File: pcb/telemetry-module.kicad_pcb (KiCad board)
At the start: 2 copper layers, 45.5 x 30 mm, 8 parts, among them J1 ODU Diagnostic Port, J3 5V-3.3V Level Shifter, J4 XIAO ESP32S3, J5 ODU 5V power jumper

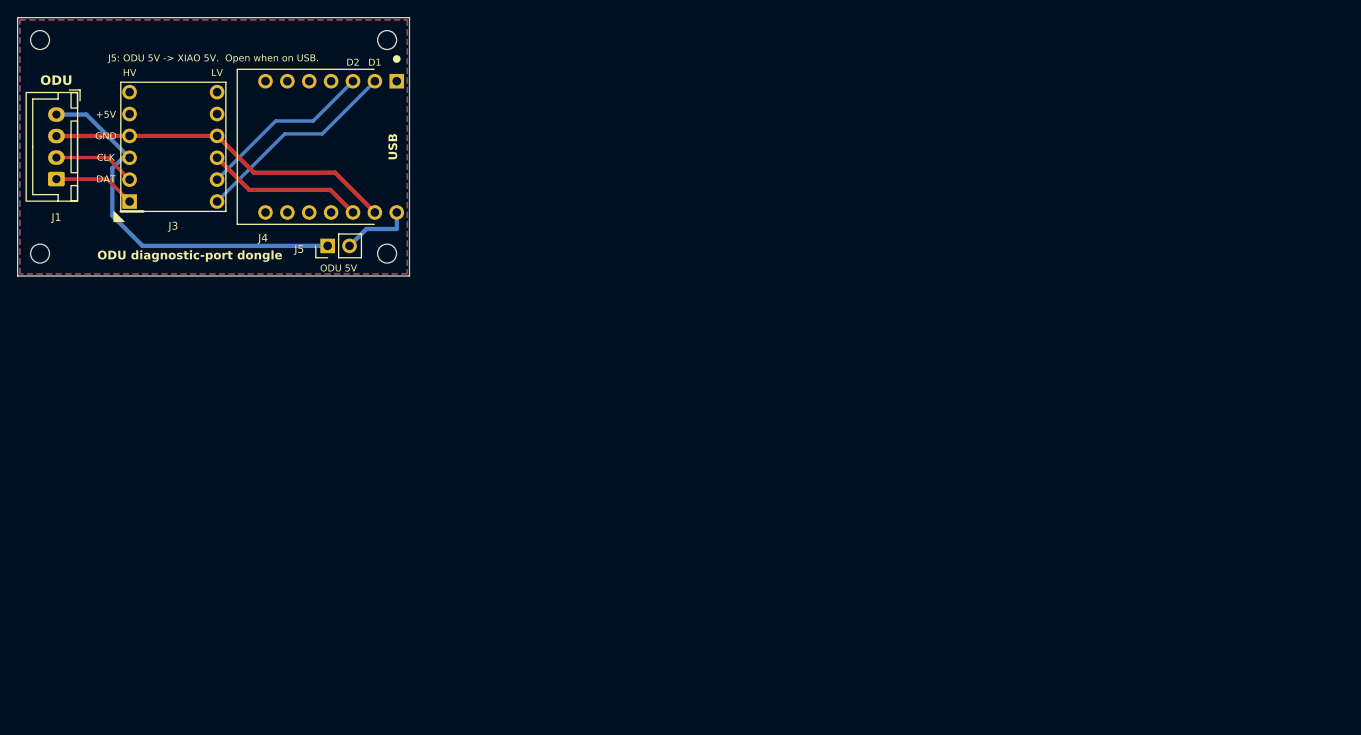
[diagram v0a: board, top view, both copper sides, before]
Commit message: GH-0014: reduce size of PCB
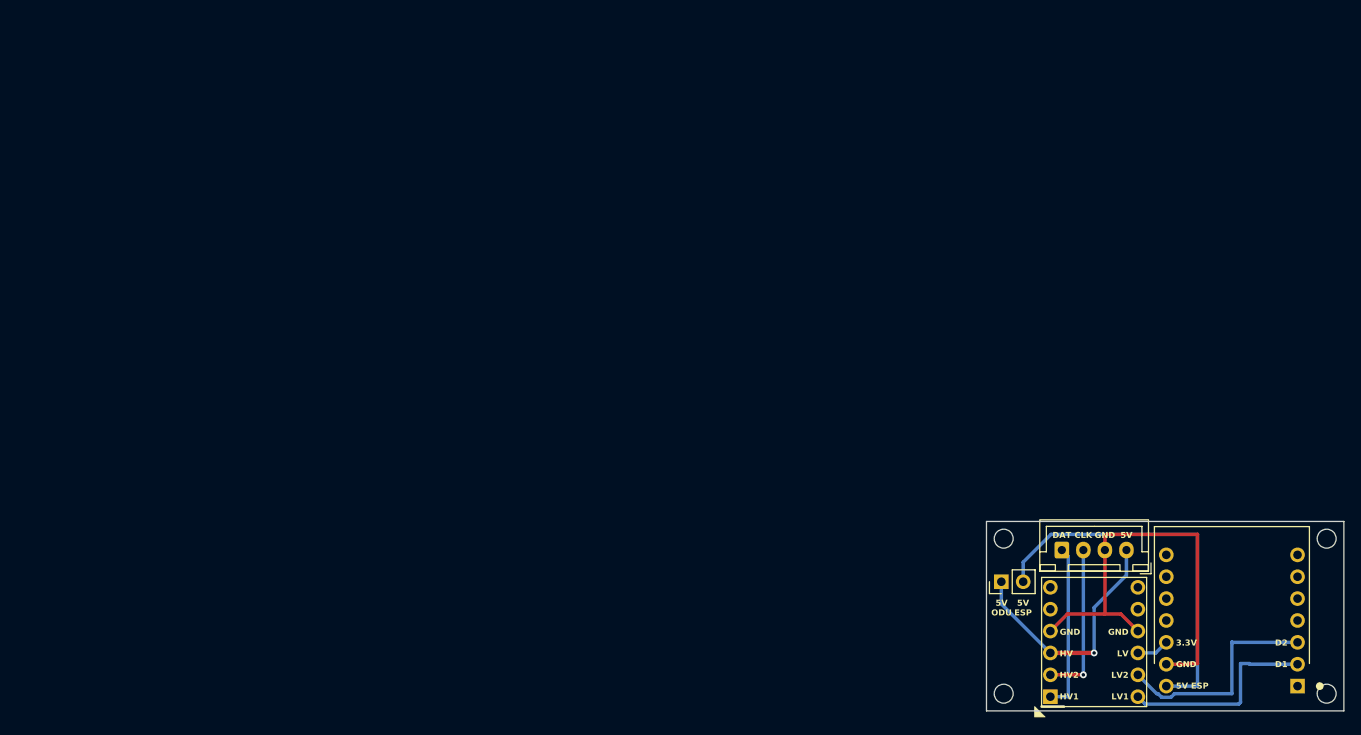
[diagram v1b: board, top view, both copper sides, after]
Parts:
- moved H1 126.0 mm to (114.5, 60.5)
- moved J1 124.4 mm to (121.2, 61.8), turned to 0 degrees
- moved H3 123.5 mm to (152.0, 60.5)
- moved H2 123.0 mm to (114.5, 78.5)
- moved J3 121.4 mm to (125.0, 72.5)
- moved H4 120.5 mm to (152.0, 78.5)
- moved J4 118.2 mm to (141.0, 70.0), turned to -90 degrees
- moved J5 87.4 mm to (114.2, 65.5)
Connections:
- net /GND renamed GND
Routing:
- net /XIAO_5V: track 8.21 -> 45.1 mm
- net /ODU_5V: track 45.0 -> 29.2 mm, vias 0 -> 1
- net /+3V3: track 18.4 -> 3.81 mm
- net GND: track 40.7 -> 51.0 mm
- net /DAT_5V: track 9.58 -> 19.4 mm
- net /CLK_5V: track 9.56 -> 18.3 mm, vias 0 -> 1
- net /CLK_3V3: track 20.5 -> 25.8 mm
- net /DAT_3V3: track 24.1 -> 23.5 mm
- removed copper zone on B.Cu, net GND
- removed copper zone on F.Cu, net GND
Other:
- board size 45.5 x 30 mm -> 41.5 x 22 mm
- board text added: "3.3V"
- board text added: "5V"
- board text added: "5V ESP"
- board text added: "5V ODU"
- board text added: "HV1"
- board text added: "HV2"
- board text added: "LV1"
- board text added: "LV2"
- board text removed: "+5V"
- board text removed: "J5: ODU 5V -> XIAO 5V. Open when on USB."
- board text removed: "ODU"
- board text removed: "ODU 5V"
- board text removed: "ODU diagnostic-port dongle"
- board text removed: "USB"
